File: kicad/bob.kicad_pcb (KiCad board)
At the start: 2 copper layers, 47 x 18.4 mm, 45 parts, among them J1 GPIO (Optional), J2 Mini USB Female, J3 Battery Connector, J4 GPIO (Optional), SW1 Screw Switch, U1 RP2040, U2 W25Q64JVSS, U3 NCP1117-3.3_SOT223, U4 MPU-6050, U5 BMP180, Y1 12MHz

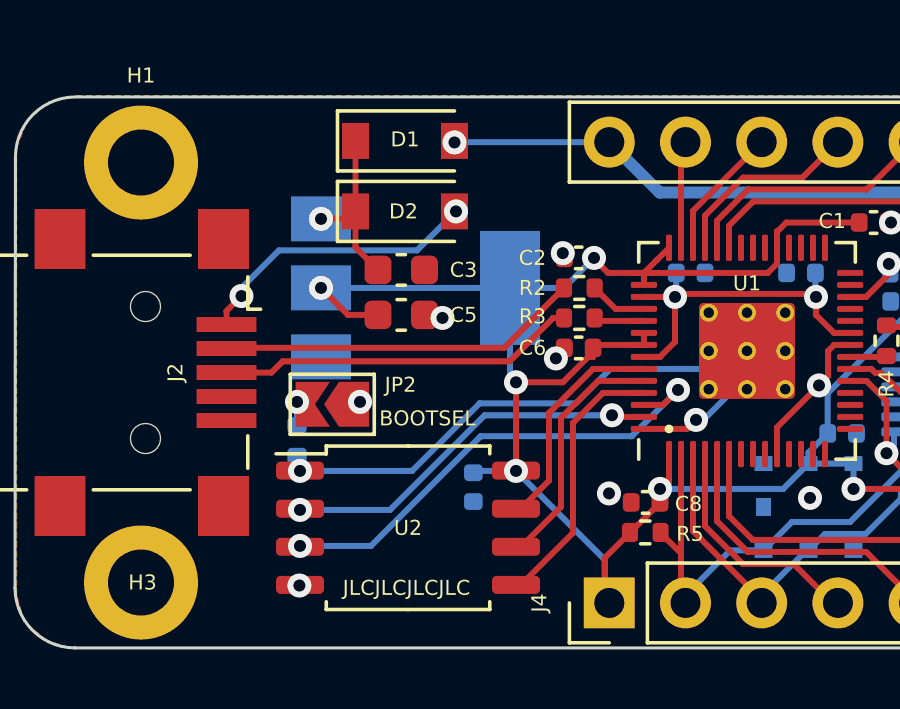
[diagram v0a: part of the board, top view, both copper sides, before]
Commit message: Fixed issues with USB impedance
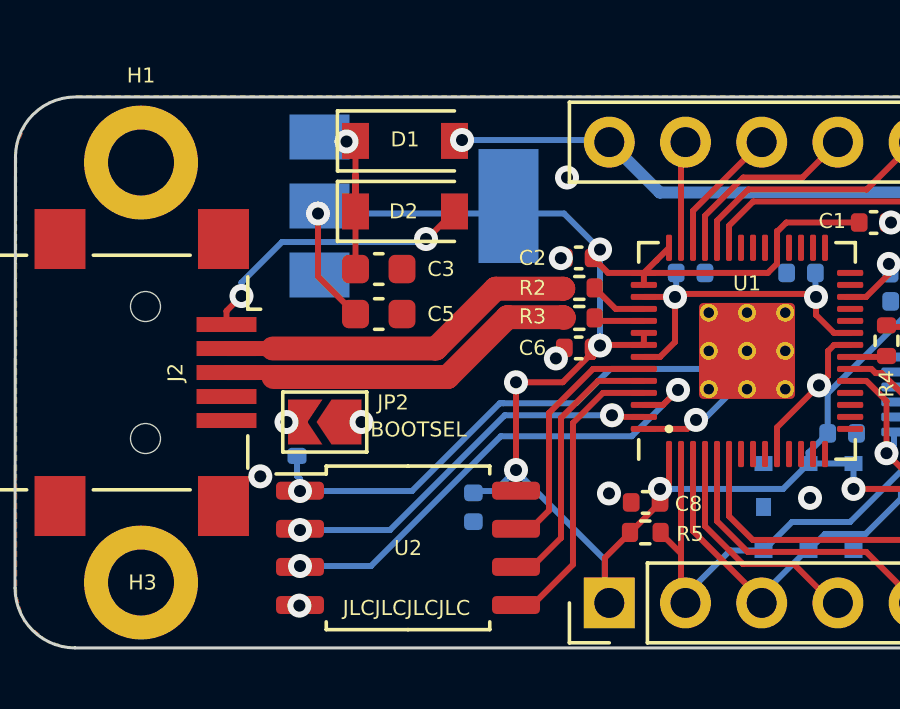
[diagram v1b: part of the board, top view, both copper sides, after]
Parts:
- moved U3 2.73 mm to (31.6, 19.9)
- moved C3 0.75 mm to (30.4, 22.1)
- moved C5 0.75 mm to (30.4, 23.6)
- moved C15 0.67 mm to (33.6, 30.0)
- moved U2 0.67 mm to (31.4, 31.3)
- moved JP2 0.64 mm to (28.6, 27.1)
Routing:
- net +3V3: track 96.3 -> 99.6 mm, vias 9 -> 10
- net QSPI_SS: track 20.1 -> 21.1 mm
- net QSPI_SD0: track 9.06 -> 9.96 mm
- net QSPI_SCLK: track 8.29 -> 9.17 mm
- net QSPI_SD3: track 7.51 -> 8.37 mm
- net Net-(JP2-Pad2): track 0.78 -> 0.20 mm
- net GND: vias 10 -> 11

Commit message: Rev 3, issued for production
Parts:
- removed the YAR at (22.6, 25.5)
- added BZ1: Buzzer, Buzzer_Beeper:Buzzer_12x9.5RM7.6, F.Cu at (60.7, 40.6)
- added C17: 220n, Capacitor_SMD:C_0603_1608Metric, F.Cu at (56.5, 27.1)
- added C18: 100n, Capacitor_SMD:C_0603_1608Metric, F.Cu at (65.0, 25.4)
- added J5: Conn_01x03_Male, Connector_PinHeader_2.54mm:PinHeader_1x02_P2.54mm_Vertical, B.Cu at (55.1, 29.2)
- added TP1: TestPoint, TestPoint:TestPoint_Pad_D1.0mm, B.Cu at (51.2, 24.1)
- added TP2: TestPoint, TestPoint:TestPoint_Pad_D1.0mm, B.Cu at (51.2, 25.9)
- added TP3: TestPoint, TestPoint:TestPoint_Pad_D1.0mm, B.Cu at (51.2, 27.6)
- added TP4: TestPoint, TestPoint:TestPoint_Pad_D1.0mm, B.Cu at (51.2, 29.4)
- added U6: HP203B, RP2040_minimal:LGA-8_3.6x3.8x0.9P, F.Cu at (61.6, 27.1)
- added YAR: LOGO, Logos:YAR_Logo, F.Cu at (28.2, 30.5)
- C1, C8: footprint Capacitor_SMD:C_0402_1005Metric -> Capacitor_SMD:C_0603_1608Metric
- C10: value 100n -> 4p; footprint Capacitor_SMD:C_0402_1005Metric -> Capacitor_SMD:C_0603_1608Metric; moved to F.Cu
- C11, C12, C14, C15: footprint Capacitor_SMD:C_0402_1005Metric -> Capacitor_SMD:C_0603_1608Metric; moved to F.Cu
- C13: value 1u -> 4p; footprint Capacitor_SMD:C_0402_1005Metric -> Capacitor_SMD:C_0603_1608Metric; moved to F.Cu
- C16: value 1u -> 4.7u; footprint Capacitor_SMD:C_0402_1005Metric -> Capacitor_SMD:C_0603_1608Metric; moved to F.Cu
- C2: value 1u -> 10u; footprint Capacitor_SMD:C_0402_1005Metric -> Capacitor_SMD:C_0603_1608Metric
- C3: value 10u -> 1u
- C4: value 100n -> 1u; footprint Capacitor_SMD:C_0402_1005Metric -> Capacitor_SMD:C_0603_1608Metric; moved to F.Cu
- C5: value 10u -> 100n
- C6: value 100n -> 10u; footprint Capacitor_SMD:C_0402_1005Metric -> Capacitor_SMD:C_0603_1608Metric
- C7, C9: value 27p -> 100n; footprint Capacitor_SMD:C_0402_1005Metric -> Capacitor_SMD:C_0603_1608Metric
- J1: value GPIO (Optional) -> Mini USB Female; footprint Connector_PinHeader_2.54mm:PinHeader_1x07_P2.54mm_Vertical -> Connector_USB:USB_Mini-B_Lumberg_2486_01_Horizontal
- J2: value Mini USB Female -> GPIO (Optional); footprint Connector_USB:USB_Mini-B_Lumberg_2486_01_Horizontal -> Connector_PinHeader_2.54mm:PinHeader_1x07_P2.54mm_Vertical_NoSilk
- J3: value Battery Connector -> GPIO (Optional); footprint Connector_Wire:Compact_Relief -> Connector_PinHeader_2.54mm:PinHeader_1x07_P2.54mm_Vertical_NoSilk
- J4: value GPIO (Optional) -> Battery Connector; footprint Connector_PinHeader_2.54mm:PinHeader_1x07_P2.54mm_Vertical -> Connector_Wire:Compact_Relief; moved to B.Cu
- JP1: value RESET -> BOOTSEL; footprint Jumper:SolderJumper-2_P1.3mm_Open_TrianglePad1.0x1.5mm -> Jumper:SolderJumper-2_P1.3mm_Open_RoundedPad1.0x1.5mm
- JP2: value BOOTSEL -> RESET; footprint Jumper:SolderJumper-2_P1.3mm_Open_TrianglePad1.0x1.5mm -> Jumper:SolderJumper-2_P1.3mm_Open_RoundedPad1.0x1.5mm
- R1: value 1k -> 27; footprint Resistor_SMD:R_0402_1005Metric -> Resistor_SMD:R_0603_1608Metric_Pad0.98x0.95mm_HandSolder; moved to F.Cu
- R2: footprint Resistor_SMD:R_0402_1005Metric -> Resistor_SMD:R_0603_1608Metric_Pad0.98x0.95mm_HandSolder
- R3: value 27 -> 1k; footprint Resistor_SMD:R_0402_1005Metric -> Resistor_SMD:R_0603_1608Metric
- R4: footprint Resistor_SMD:R_0402_1005Metric -> Resistor_SMD:R_0603_1608Metric
- R5: value 4k7 -> 1k; footprint Resistor_SMD:R_0402_1005Metric -> Resistor_SMD:R_0603_1608Metric
- R6: value 1k -> 10k; footprint Resistor_SMD:R_0402_1005Metric -> Resistor_SMD:R_0603_1608Metric; moved to F.Cu
- R7: value 4k7 -> 10k; footprint Resistor_SMD:R_0402_1005Metric -> Resistor_SMD:R_0603_1608Metric; moved to F.Cu
- R8: value 1k -> 100; footprint Resistor_SMD:R_0402_1005Metric -> Resistor_SMD:R_0603_1608Metric; moved to F.Cu
- SW1: footprint Connector:Screw_Switch_M3 -> Connector:Screw_Switch_M2
- U1: value RP2040 -> W25Q64JVSS; footprint RP2040_minimal:RP2040-QFN-56 -> Package_SO:SOIC-8_5.23x5.23mm_P1.27mm
- U2: value W25Q64JVSS -> AMS1117-3.3; footprint Package_SO:SOIC-8_5.23x5.23mm_P1.27mm -> Package_TO_SOT_SMD:SOT-223-3_TabPin2
- U3: value NCP1117-3.3_SOT223 -> RP2040; footprint Package_TO_SOT_SMD:SOT-223-3_TabPin2 -> RP2040_minimal:RP2040-QFN-56_HS; moved to F.Cu
- U4: value MPU-6050 -> QMC5883L; footprint Sensor_Motion:InvenSense_QFN-24_4x4mm_P0.5mm -> Silicon-Custom:LGA-16-3X3; moved to F.Cu
- U5: value BMP180 -> QMI8658C; footprint Silicon-Custom:BMP180 -> Silicon-Custom:14LGA_2.5x3.0; moved to F.Cu
- moved H2 49.7 mm to (16.5, 40.6)
- moved H3 48.9 mm to (69.8, 20.3)
- moved R6 37.7 mm to (65.0, 22.4), turned to 0 degrees
- moved J1 37.7 mm to (17.9, 30.5)
- moved J4 33.1 mm to (71.1, 34.9), turned to 180 degrees
- moved C1 32.9 mm to (21.3, 41.1), turned to 180 degrees
- moved J3 30.5 mm to (35.6, 41.9)
- moved C15 23.8 mm to (56.5, 23.7), turned to 0 degrees
- moved JP1 22.3 mm to (35.4, 38.6), turned to 0 degrees
- moved U1 20.8 mm to (27.9, 39.4), turned to 180 degrees
- moved JP2 19.0 mm to (47.1, 22.6)
- moved U5 18.1 mm to (61.6, 23.2), turned to 90 degrees
- moved C4 17.6 mm to (34.3, 27.7)
- moved R7 17.5 mm to (65.0, 23.9)
- moved C13 17.4 mm to (52.6, 35.1)
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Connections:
- C10 pad 1: Net-(C10-Pad1) -> GND
- C10 pad 2: GND -> XIN
- C11 pad 1: +3V3 -> +1V1
- C12 pad 1: +1V1 -> +3V3
- C13 pad 1: +1V1 -> GND
- C13 pad 2: GND -> Net-(C4-Pad2)
- C16 pad 1: Net-(C16-Pad1) -> Net-(C99-Pad1)
- C2 pad 1: +3V3 -> Net-(C16-Pad1)
- C3 pad 1: Net-(D2-Pad1) -> +3V3
- C4 pad 1: +3V3 -> +1V1
- C7 pad 1: GND -> +3V3
- C7 pad 2: Net-(C7-Pad2) -> GND
- C9 pad 1: GND -> +3V3
- C9 pad 2: XIN -> GND
- D1 pad 1: Net-(D2-Pad1) -> Net-(C16-Pad1)
- D1 pad 2: +BATT -> VBUS
- D2 pad 1: Net-(D2-Pad1) -> Net-(C16-Pad1)
- D2 pad 2: VBUS -> +BATT
- J1 pad 1: GND -> VBUS
- J1 pad 2: GPIO25 -> USB_D-
- J1 pad 3: GPIO26 -> USB_D+
- J1 pad 4: GPIO27 -> unconnected-(J3-Pad4)
- J1 pad 5: GPIO28 -> GND
- J1 pad 6: GPIO29 -> GND
- J2 pad 2: USB_D- -> +BATT
- J2 pad 3: USB_D+ -> GPIO29
- J2 pad 4: unconnected-(J2-Pad4) -> GPIO28
- J2 pad 5: GND -> GPIO27
- J2 pad 6: GND -> GPIO26
- J3 pad 1: GND -> +3V3
- J3 pad 2: Net-(J3-Pad2) -> GPIO0
- J4 pad 1: +3V3 -> GND
- J4 pad 2: I2C_SDA -> Net-(J1-Pad2)
- R1 pad 1: +3V3 -> Net-(R8-Pad1)
- R1 pad 2: Net-(JP1-Pad2) -> USB_D-
- R2 pad 1: Net-(U1-Pad46) -> Net-(R7-Pad1)
- R2 pad 2: USB_D- -> USB_D+
- R3 pad 1: Net-(R3-Pad1) -> Net-(JP1-Pad2)
- R3 pad 2: USB_D+ -> QSPI_SS
- R4 pad 1: Net-(C7-Pad2) -> +3V3
- R4 pad 2: XOUT -> Net-(JP2-Pad2)
- R5 pad 1: I2C_SDA -> Net-(C4-Pad2)
- R5 pad 2: +3V3 -> XOUT
- R6 pad 1: Net-(JP2-Pad2) -> I2C_SDA
- R6 pad 2: QSPI_SS -> +3V3
- SW1 pad 1: Net-(J3-Pad2) -> Net-(J1-Pad2)
- U1 pad 1: +3V3 -> QSPI_SS
- U1 pad 2: I2C_SDA -> QSPI_SD1
- U1 pad 3: I2C_SCL -> QSPI_SD2
- U1 pad 4: GPIO2 -> GND
- U1 pad 5: GPIO3 -> QSPI_SD0
- U1 pad 6: GPIO4 -> QSPI_SCLK
- U1 pad 7: unconnected-(U1-Pad7) -> QSPI_SD3
- U1 pad 8: unconnected-(U1-Pad8) -> +3V3
- U2 pad 1: QSPI_SS -> GND
- U2 pad 2: QSPI_SD1 -> +3V3
- U2 pad 3: QSPI_SD2 -> Net-(C16-Pad1)
- U3 pad 1: GND -> +3V3
- U3 pad 2: +3V3 -> GPIO0
- U3 pad 3: Net-(D2-Pad1) -> GPIO1
- U4 pad 1: GND -> I2C_SCL
- U4 pad 10: Net-(C10-Pad1) -> Net-(C99-Pad1)
- U4 pad 12: unconnected-(U4-Pad12) -> Net-(C100-Pad2)
- U4 pad 16: unconnected-(U4-Pad16) -> I2C_SDA
- U4 pad 2: unconnected-(U4-Pad2) -> +3V3
- U4 pad 4: unconnected-(U4-Pad4) -> +3V3
- U4 pad 8: +3V3 -> Net-(C100-Pad1)
- U5 pad 1: (no net) -> GND
- U5 pad 2: +3V3 -> GND
- U5 pad 3: +3V3 -> GND
- U5 pad 4: (no net) -> unconnected-(U8-Pad4)
- U5 pad 5: I2C_SCL -> +3V3
- U5 pad 6: I2C_SDA -> GND
- Y1 pad 1: Net-(C7-Pad2) -> Net-(C4-Pad2)
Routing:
- net +3V3: track 99.6 -> 149.1 mm
- net +BATT: track 25.4 -> 59.1 mm
- net BUZZER: track 0.00 -> 23.2 mm
- net VBUS: track 9.42 -> 26.1 mm, vias 2 -> 1
- net I2C_SDA: track 16.1 -> 29.3 mm, vias 0 -> 4
- net I2C_SCL: track 14.1 -> 26.8 mm, vias 0 -> 4
- net +1V1: track 12.2 -> 23.4 mm, vias 2 -> 0
- net GPIO25: track 10.6 -> 0.00 mm
- net QSPI_SD3: track 8.37 -> 18.9 mm
- net SWCLK: track 0.00 -> 10.4 mm
- net QSPI_SCLK: track 9.17 -> 19.1 mm, vias 0 -> 2
- net GPIO0: track 0.00 -> 9.02 mm
- net Net-(JP2-Pad2): track 0.20 -> 9.22 mm, vias 1 -> 2
- net GND: track 11.0 -> 2.39 mm, vias 11 -> 22
- net Net-(C7-Pad2): track 8.45 -> 0.00 mm
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- added copper zone on F.Cu, net +3V3
- added copper zone on B.Cu, net +BATT
- added copper zone on F.Cu, net Net-(C16-Pad1)
- added copper zone on F.Cu, net Net-(J1-Pad2)
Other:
- board size 47 x 18.4 mm -> 58.4 x 25.4 mm
- board text added: "0"
- board text added: "1"
- board text added: "2"
- board text added: "26"
- board text added: "27"
- board text added: "28"
- board text added: "29"
- board text added: "3"
- board text added: "3V3"
- board text added: "3v3"
- board text added: "4"
- board text added: "Bob Rev 3"
- board text added: "GND"
- board text added: "MAX 12VDC"
- board text added: "SCL"
- board text added: "SDA"
- board text added: "SWCLK"
- board text added: "SWD"
- board text added: "Sensitive Crystal Do not route underneath"
- board text added: "USB Requires GND underneath"
- board text added: "VBAT"
- board text added: "VBUS"
- board text added: "X"
- board text added: "Y"
- board text added: "Z"
- board text removed: "Bob Rev 2"

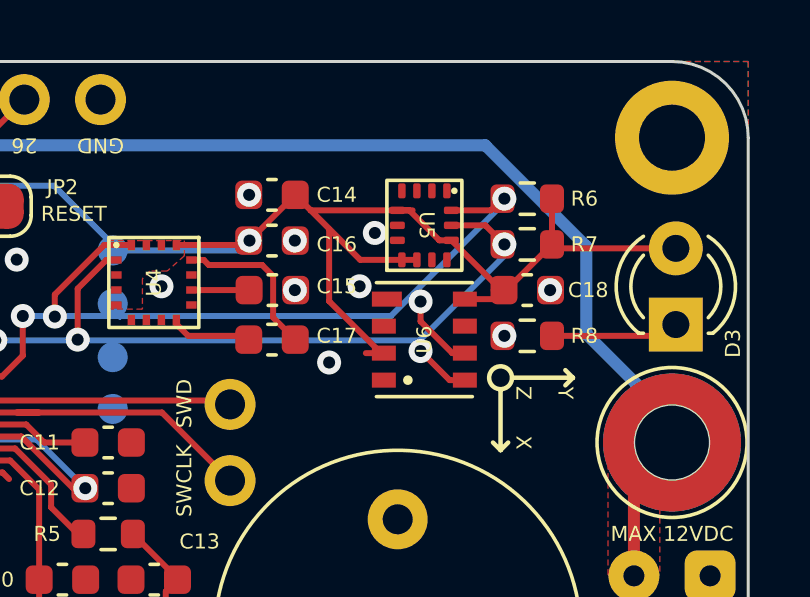
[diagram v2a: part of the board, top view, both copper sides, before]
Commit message: Fixed issues and reissued for production
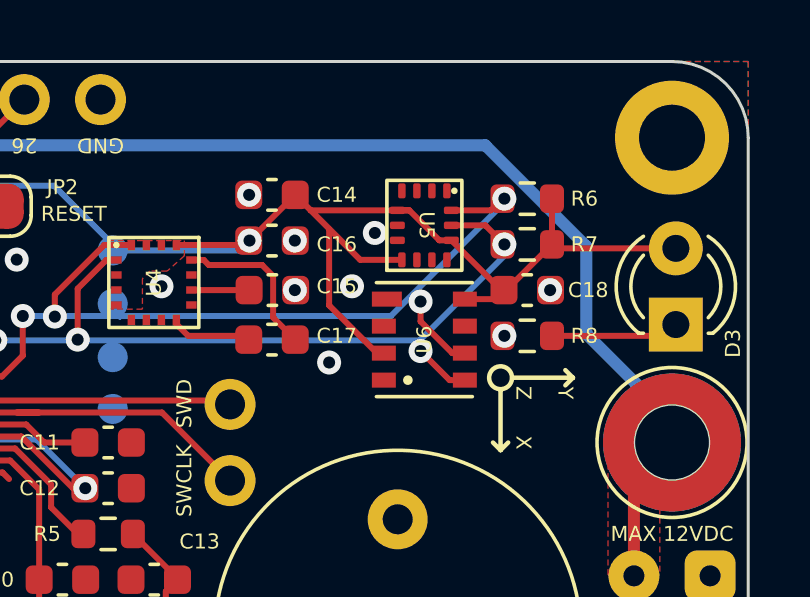
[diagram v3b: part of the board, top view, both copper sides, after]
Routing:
- net +3V3: track 149.1 -> 147.0 mm
- net GND: vias 22 -> 23
- net (no net): vias 1 -> 0
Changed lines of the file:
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@@
     (effects (font (size 0.5 0.5) (thickness 0.125)))
   )
-  (via (at 23.5712 25.654) (size 0.8) (drill 0.4) (layers "F.Cu" "B.Cu") (free) (net 0))
   (segment (start 46.78 31.48) (end 47.5328 31.48) (width 0.2) (layer "F.Cu") (net 1))
   (segment (start 45.72 31.75) (end 45.72 31.9024) (width 0.2) (layer "F.Cu") (net 1))
@@
   (via (at 52.832 25.273) (size 0.8) (drill 0.4) (layers "F.Cu" "B.Cu") (free) (net 1))
   (via (at 37.2364 35.6108) (size 0.8) (drill 0.4) (layers "F.Cu" "B.Cu") (free) (net 1))
+  (via (at 23.5712 25.654) (size 0.8) (drill 0.4) (layers "F.Cu" "B.Cu") (free) (net 1))
   (via (at 27.8384 19.7612) (size 0.8) (drill 0.4) (layers "F.Cu" "B.Cu") (free) (net 1))
   (via (at 45.507737 32.680737) (size 0.8) (drill 0.4) (layers "F.Cu" "B.Cu") (free) (net 1))
   (via (at 37.7952 25.0952) (size 0.8) (drill 0.4) (layers "F.Cu" "B.Cu") (free) (net 1))
   (via (at 24.4348 32.8168) (size 0.8) (drill 0.4) (layers "F.Cu" "B.Cu") (free) (net 1))
-  (via (at 59.436 25.273) (size 0.8) (drill 0.4) (layers "F.Cu" "B.Cu") (free) (net 1))
+  (via (at 59.182 25.273) (size 0.8) (drill 0.4) (layers "F.Cu" "B.Cu") (free) (net 1))
   (via (at 32.004 24.7396) (size 0.8) (drill 0.4) (layers "F.Cu" "B.Cu") (free) (net 1))
   (via (at 55.753 22.225) (size 0.8) (drill 0.4) (layers "F.Cu" "B.Cu") (net 1))
@@
   (segment (start 37.183 28.28) (end 39.58 28.28) (width 0.2) (layer "F.Cu") (net 3))
   (segment (start 39.58 28.28) (end 39.58 27.88) (width 0.2) (layer "F.Cu") (net 3))
-  (segment (start 60.245 27.501) (end 59.645 27.501) (width 0.2) (layer "F.Cu") (net 3))
   (segment (start 44.18 26.88) (end 44.18 24.648) (width 0.2) (layer "F.Cu") (net 3))
+  (segment (start 58.42 25.908) (end 58.42 23.368) (width 0.2) (layer "F.Cu") (net 3))
   (segment (start 44.18 37.081) (end 44.183 37.084) (width 0.2) (layer "F.Cu") (net 3))
   (segment (start 35.065 32.258) (end 35.922693 32.258) (width 0.2) (layer "F.Cu") (net 3))
@@
   (segment (start 49.88165 32.004) (end 50.279 32.004) (width 0.2) (layer "F.Cu") (net 3))
   (segment (start 35.922693 32.258) (end 37.900693 30.28) (width 0.2) (layer "F.Cu") (net 3))
+  (segment (start 60.153 27.501) (end 60.013 27.501) (width 0.2) (layer "F.Cu") (net 3))
   (segment (start 51.328 24.896) (end 51.332 24.892) (width 0.2) (layer "F.Cu") (net 3))
   (segment (start 39.57952 29.87952) (end 39.58 29.88) (width 0.2) (layer "F.Cu") (net 3))
-  (segment (start 61.353 24.391) (end 59.456 24.391) (width 0.2) (layer "F.Cu") (net 3))
   (segment (start 43.1355 22.1295) (end 43.104 22.098) (width 0.2) (layer "F.Cu") (net 3))
   (segment (start 59.456 24.391) (end 57.806 22.741) (width 0.2) (layer "F.Cu") (net 3))
@@
   (segment (start 55.74 23.749) (end 55.766 23.749) (width 0.2) (layer "F.Cu") (net 3))
   (segment (start 39.58 27.88) (end 40.58 26.88) (width 0.2) (layer "F.Cu") (net 3))
-  (segment (start 63.948 25.701) (end 64.249 25.4) (width 0.2) (layer "F.Cu") (net 3))
   (segment (start 38.301173 29.87952) (end 39.57952 29.87952) (width 0.2) (layer "F.Cu") (net 3))
-  (segment (start 60.695 22.741) (end 61.095 22.741) (width 0.2) (layer "F.Cu") (net 3))
+  (segment (start 59.456 24.391) (end 60.845 24.391) (width 0.2) (layer "F.Cu") (net 3))
   (segment (start 55.593 23.896) (end 55.74 23.749) (width 0.2) (layer "F.Cu") (net 3))
   (segment (start 46.78 30.28) (end 48.15765 30.28) (width 0.2) (layer "F.Cu") (net 3))
-  (segment (start 58.42 25.768) (end 58.42 23.368) (width 0.2) (layer "F.Cu") (net 3))
+  (segment (start 60.013 27.501) (end 58.42 25.908) (width 0.2) (layer "F.Cu") (net 3))
   (segment (start 65.981 24.008) (end 69.977 24.008) (width 0.2) (layer "F.Cu") (net 3))
   (segment (start 37.900693 30.28) (end 38.301173 29.87952) (width 0.2) (layer "F.Cu") (net 3))
   (segment (start 44.18 24.648) (end 43.154 23.622) (width 0.2) (layer "F.Cu") (net 3))
-  (segment (start 60.153 27.501) (end 58.42 25.768) (width 0.2) (layer "F.Cu") (net 3))
   (segment (start 64.154 25.4) (end 62.495 23.741) (width 0.2) (layer "F.Cu") (net 3))
-  (segment (start 64.249 25.4) (end 63.9 25.4) (width 0.2) (layer "F.Cu") (net 3))
-  (segment (start 64.249 25.4) (end 64.325 25.4) (width 0.2) (layer "F.Cu") (net 3))
   (segment (start 48.15765 30.28) (end 49.88165 32.004) (width 0.2) (layer "F.Cu") (net 3))
   (segment (start 44.18 34.08) (end 44.18 37.081) (width 0.2) (layer "F.Cu") (net 3))
-  (segment (start 61.203 22.741) (end 57.806 22.741) (width 0.2) (layer "F.Cu") (net 3))
-  (segment (start 61.095 22.741) (end 62.095 23.741) (width 0.2) (layer "F.Cu") (net 3))
   (segment (start 39.878 35.56) (end 40.58 34.858) (width 0.2) (layer "F.Cu") (net 3))
   (segment (start 22.111 41.148) (end 24.213 41.148) (width 0.2) (layer "F.Cu") (net 3))
+  (segment (start 60.695 22.741) (end 61.095 22.741) (width 0.2) (layer "F.Cu") (net 3))
+  (segment (start 62.095 23.741) (end 62.495 23.741) (width 0.2) (layer "F.Cu") (net 3))
   (segment (start 65.849 23.876) (end 65.981 24.008) (width 0.2) (layer "F.Cu") (net 3))
   (segment (start 65.849 23.876) (end 65.849 22.352) (width 0.2) (layer "F.Cu") (net 3))
   (segment (start 55.766 23.749) (end 57.29 22.225) (width 0.2) (layer "F.Cu") (net 3))
   (segment (start 37.900693 30.28) (end 39.58 30.28) (width 0.2) (layer "F.Cu") (net 3))
-  (segment (start 62.095 23.741) (end 62.495 23.741) (width 0.2) (layer "F.Cu") (net 3))
+  (segment (start 61.095 22.741) (end 62.095 23.741) (width 0.2) (layer "F.Cu") (net 3))
   (segment (start 40.58 34.858) (end 40.58 34.08) (width 0.2) (layer "F.Cu") (net 3))
   (segment (start 53.328 23.896) (end 55.593 23.896) (width 0.2) (layer "F.Cu") (net 3))
   (segment (start 35.065 26.162) (end 37.183 28.28) (width 0.2) (layer "F.Cu") (net 3))
   (segment (start 57.806 22.741) (end 57.29 22.225) (width 0.2) (layer "F.Cu") (net 3))
+  (segment (start 61.079 22.741) (end 57.806 22.741) (width 0.2) (layer "F.Cu") (net 3))
   (segment (start 62.945 25.701) (end 64.202 25.701) (width 0.2) (layer "F.Cu") (net 3))
   (via (at 39.637 35.56) (size 0.8) (drill 0.4) (layers "F.Cu" "B.Cu") (net 3))
@@
   (via (at 20.32 21.59) (size 0.8) (drill 0.4) (layers "F.Cu" "B.Cu") (net 6))
   (segment (start 39.624 20.574) (end 39.8272 20.574) (width 0.4) (layer "B.Cu") (net 6))
-  (segment (start 66.9925 26.8605) (end 66.9544 26.8224) (width 0.4) (layer "B.Cu") (net 6))
   (segment (start 39.8272 20.574) (end 36.576 20.574) (width 0.4) (layer "B.Cu") (net 6))
   (segment (start 66.9925 23.9395) (end 63.627 20.574) (width 0.4) (layer "B.Cu") (net 6))

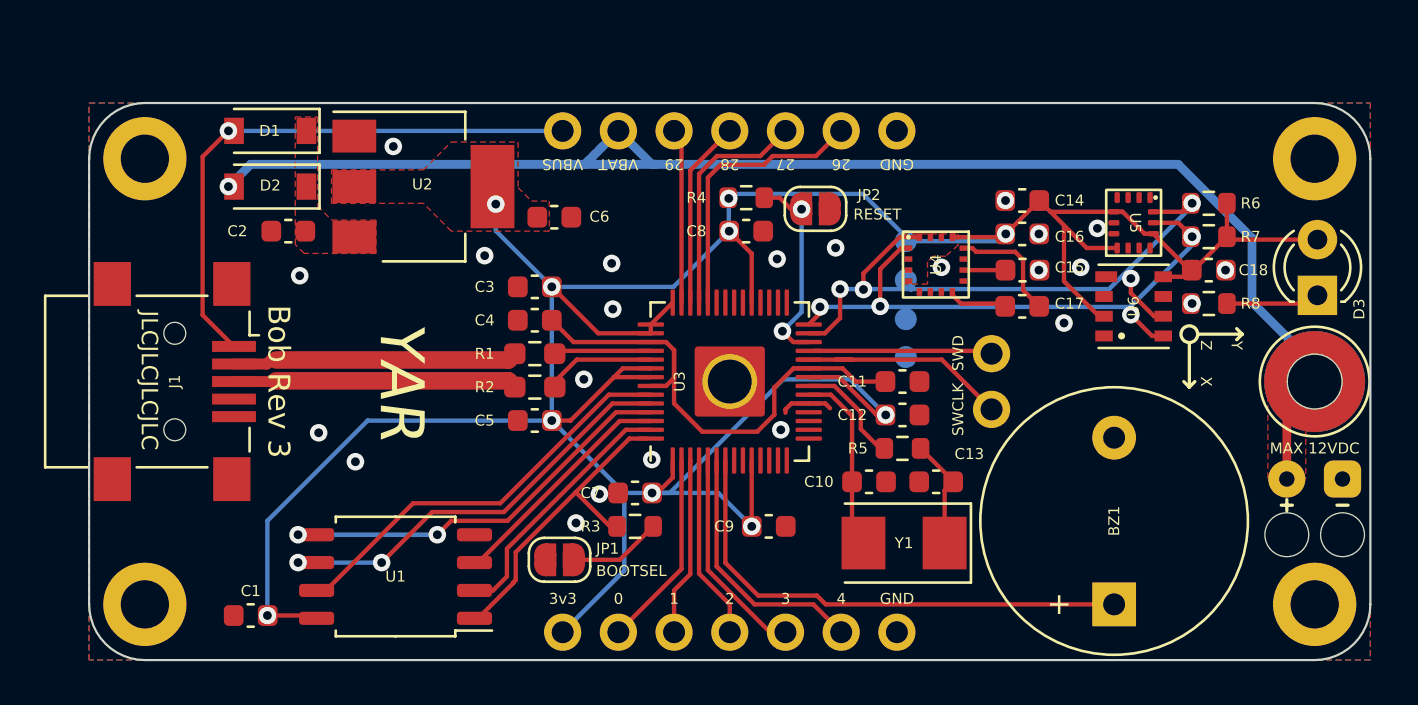
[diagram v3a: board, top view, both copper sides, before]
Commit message: Added Kicad Libs. Added thermal relief.
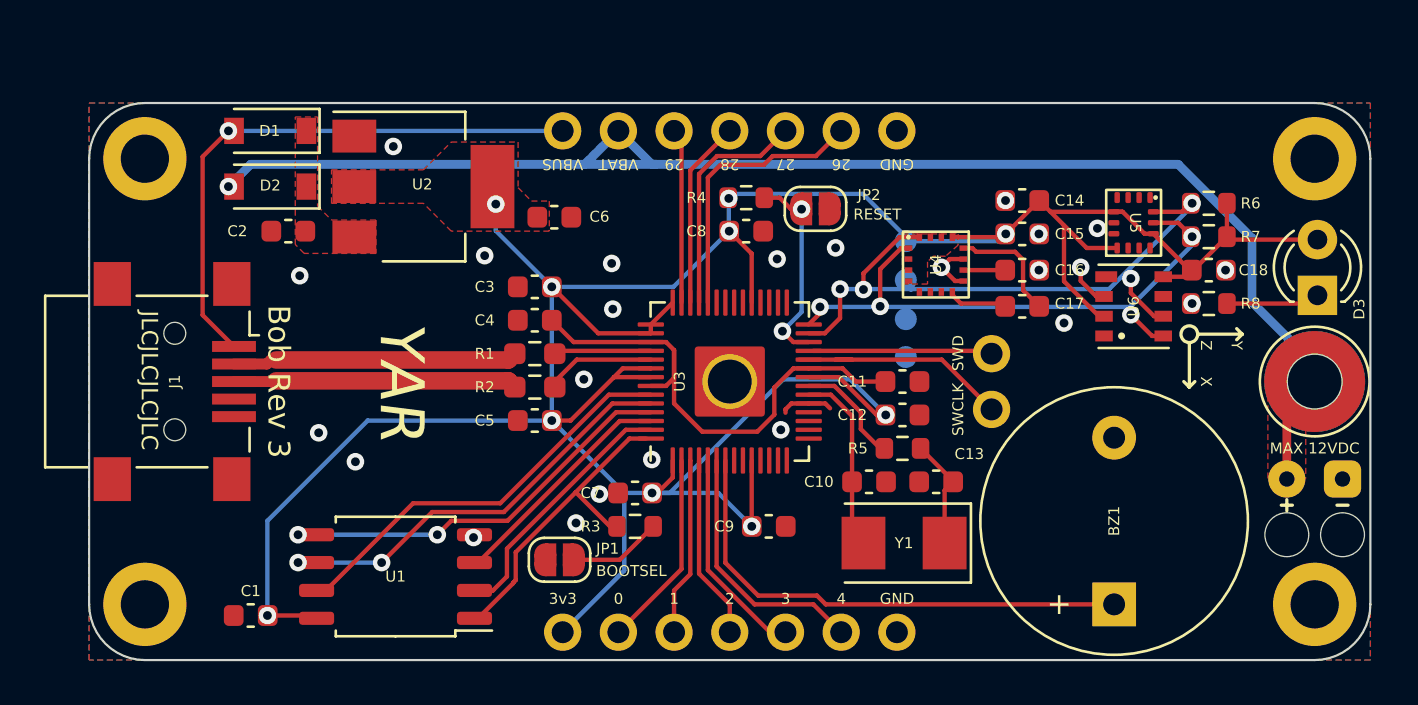
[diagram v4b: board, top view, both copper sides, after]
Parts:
- turned C16 to 180 degrees
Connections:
- C16 pad 1: Net-(C99-Pad1) -> GND
- C16 pad 2: GND -> Net-(C16-Pad2)
- U4 pad 10: Net-(C99-Pad1) -> Net-(C16-Pad2)
- U4 pad 14: unconnected-(U7-Pad14) -> (no net)
- U4 pad 3: unconnected-(U7-Pad3) -> (no net)
- U4 pad 5: unconnected-(U7-Pad5) -> (no net)
- U4 pad 6: unconnected-(U7-Pad6) -> (no net)
- U4 pad 7: unconnected-(U7-Pad7) -> (no net)
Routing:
- net GND: track 2.39 -> 6.77 mm, vias 23 -> 24
- net Net-(C99-Pad1): track 1.93 -> 0.00 mm
- net Net-(C16-Pad2): track 0.00 -> 1.93 mm
